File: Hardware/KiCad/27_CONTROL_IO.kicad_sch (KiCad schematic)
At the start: 0 parts

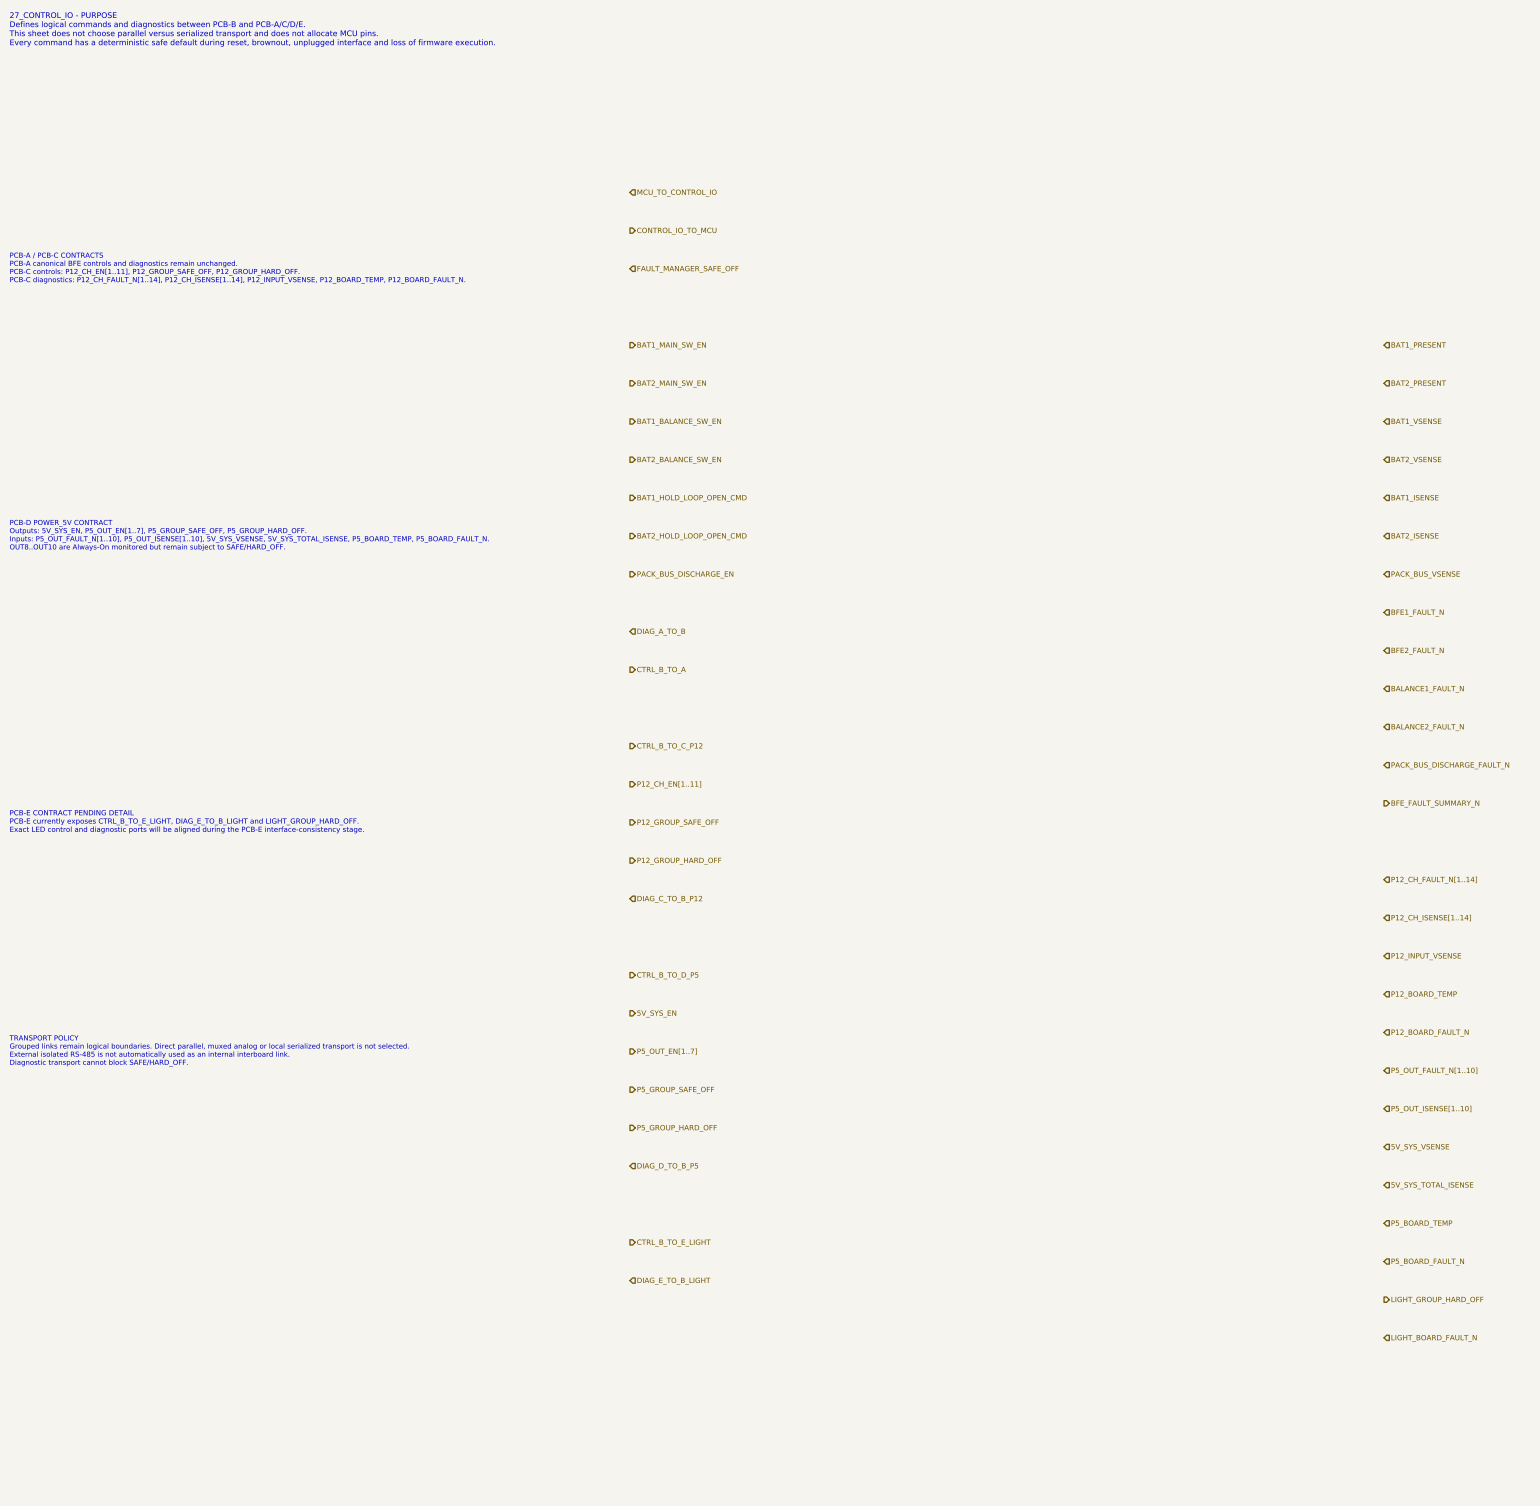
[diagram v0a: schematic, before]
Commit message: hardware: expose canonical PCB-E control and diagnostic buses
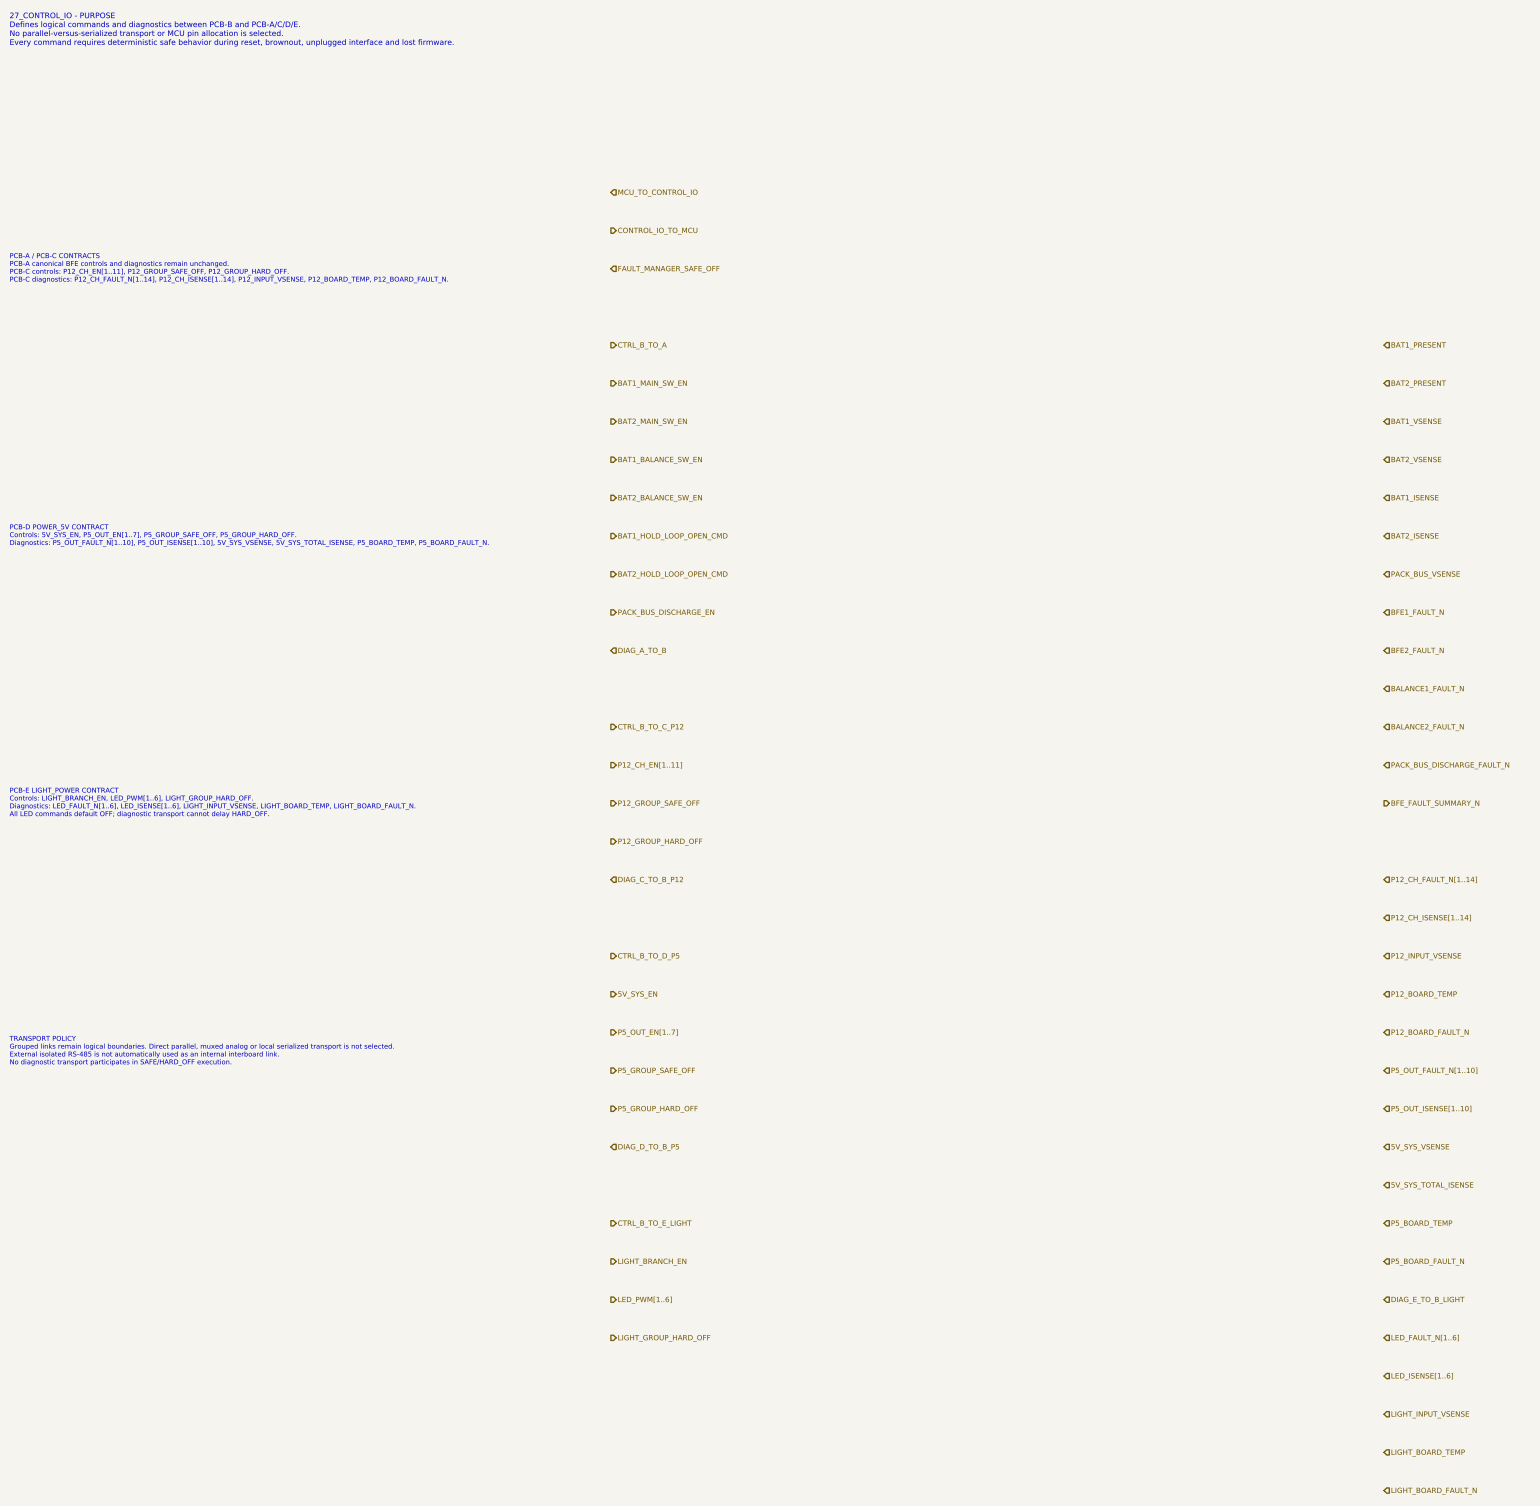
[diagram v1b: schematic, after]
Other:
- note added: "27_CONTROL_IO - PURPOSE Defines logical commands and diagnostics between PCB-B and PCB-A/C/D/E. No parallel-versus-serialized transport or MCU pin allocation is selected. Every command requires deterministic safe behavior during reset, brownout, unplugged interface and lost firmware."
- note added: "PCB-D POWER_5V CONTRACT Controls: 5V_SYS_EN, P5_OUT_EN[1..7], P5_GROUP_SAFE_OFF, P5_GROUP_HARD_OFF. Diagnostics: P5_OUT_FAULT_N[1..10], P5_OUT_ISENSE[1..10], 5V_SYS_VSENSE, 5V_SYS_TOTAL_ISENSE, P5_BOARD_TEMP, P5_BOARD_FAULT_N."
- note added: "PCB-E LIGHT_POWER CONTRACT Controls: LIGHT_BRANCH_EN, LED_PWM[1..6], LIGHT_GROUP_HARD_OFF. Diagnostics: LED_FAULT_N[1..6], LED_ISENSE[1..6], LIGHT_INPUT_VSENSE, LIGHT_BOARD_TEMP, LIGHT_BOARD_FAULT_N. All LED commands default OFF; diagnostic transport cannot delay HARD_OFF."
- note added: "TRANSPORT POLICY Grouped links remain logical boundaries. Direct parallel, muxed analog or local serialized transport is not selected. External isolated RS-485 is not automatically used as an internal interboard link. No diagnostic transport participates in SAFE/HARD_OFF execution."
- note removed: "27_CONTROL_IO - PURPOSE Defines logical commands and diagnostics between PCB-B and PCB-A/C/D/E. This sheet does not choose parallel versus serialized transport and does not allocate MCU pins. Every command has a deterministic safe default during reset, brownout, unplugged interface and loss of firmware execution."
- note removed: "PCB-D POWER_5V CONTRACT Outputs: 5V_SYS_EN, P5_OUT_EN[1..7], P5_GROUP_SAFE_OFF, P5_GROUP_HARD_OFF. Inputs: P5_OUT_FAULT_N[1..10], P5_OUT_ISENSE[1..10], 5V_SYS_VSENSE, 5V_SYS_TOTAL_ISENSE, P5_BOARD_TEMP, P5_BOARD_FAULT_N. OUT8..OUT10 are Always-On monitored but remain subject to SAFE/HARD_OFF."
- note removed: "PCB-E CONTRACT PENDING DETAIL PCB-E currently exposes CTRL_B_TO_E_LIGHT, DIAG_E_TO_B_LIGHT and LIGHT_GROUP_HARD_OFF. Exact LED control and diagnostic ports will be aligned during the PCB-E interface-consistency stage."
- note removed: "TRANSPORT POLICY Grouped links remain logical boundaries. Direct parallel, muxed analog or local serialized transport is not selected. External isolated RS-485 is not automatically used as an internal interboard link. Diagnostic transport cannot block SAFE/HARD_OFF."
